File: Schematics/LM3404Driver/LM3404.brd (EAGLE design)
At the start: 103.8 x 106.7 mm, 62 parts, among them IC1 LM3404, IC2 LM3404, IC3 LM3404, IC4 LM3404, IC5 LM3404, IC6 LM3404

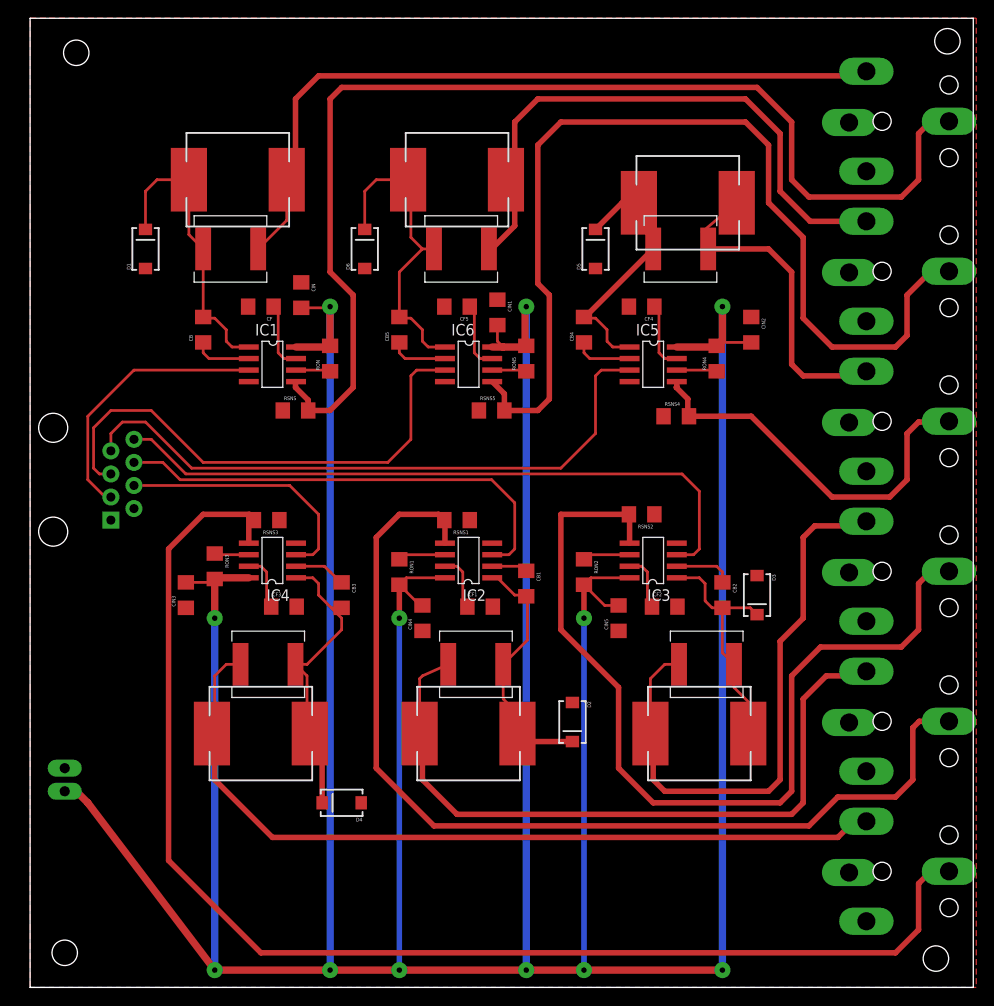
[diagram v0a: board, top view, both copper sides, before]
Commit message: Update power driver board to smt RJ45 and correct ground pins
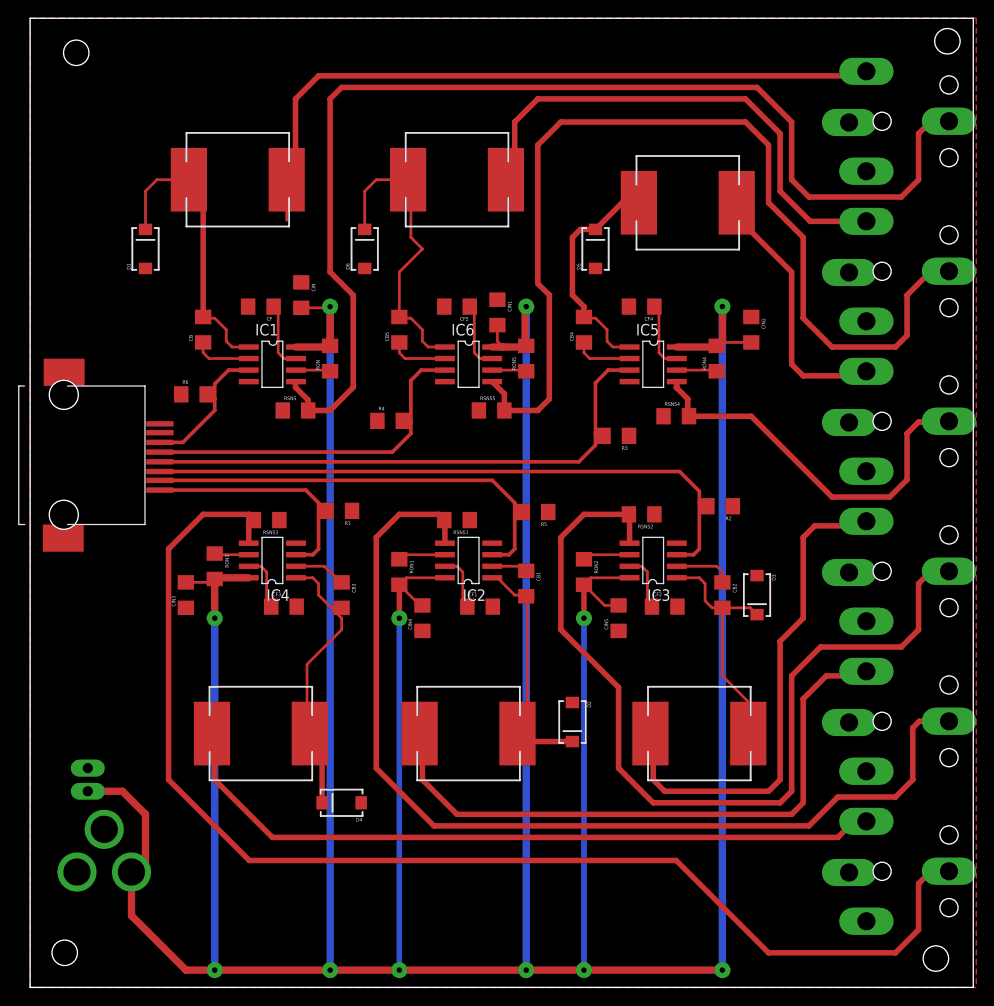
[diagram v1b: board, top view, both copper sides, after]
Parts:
- removed L1, L11, L3, L5, L7, L9: 47uH, SparkFun-Passives:CR75
- added J1: POWER_JACKPTH, SparkFun-Connectors:POWER_JACK_PTH
- added R1, R2, R3, R4, R5, R6: 4.7K, SparkFun-Resistors:1206
- U$1: value RJ45-8PTH -> MOLEX-RJ45-SMT; device SparkFun-Connectors:RJ45-8 -> SMD-RJ45:MOLEX-RJ45-SMT
- moved U$1 2.84 mm to (3.81, 58.4), flipped to the top, turned to 0 degrees
- moved POWER 2.54 mm to (6.35, 24.1)
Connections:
- net GND: now also J1.GND, J1.GNDBREAK, R1.1, R2.1, R3.1, R4.1, R5.1, R6.1
- net N$11: no longer L3.P$1
- net N$14: no longer L3.P$2
- net N$15: now also R2.2, U$1.6; no longer U$1.8
- net N$18: no longer L5.P$1
- net N$21: no longer L5.P$2
- net N$22: now also R1.2, U$1.8; no longer U$1.4
- net N$25: no longer L7.P$1
- net N$28: no longer L7.P$2
- net N$29: now also R3.2, U$1.5; no longer U$1.7
- net N$3: now also R5.2, U$1.7; no longer U$1.6
- net N$32: no longer L9.P$1
- net N$35: no longer L9.P$2
- net N$36: now also R4.2, U$1.4; no longer U$1.5
- net N$39: no longer L11.P$1
- net N$4: no longer L1.P$1
- net N$42: no longer L11.P$2
- net N$8: now also R6.2
- net N$9: no longer L1.P$2
- net VIN: now also J1.PWR
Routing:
- net N$36: track 56.7 -> 39.5 mm
- net N$8: track 30.1 -> 15.9 mm
- net N$21: track 67.5 -> 57.7 mm
- net N$14: track 78.5 -> 68.9 mm
- net N$29: track 69.8 -> 60.9 mm
- net N$28: track 90.2 -> 82.1 mm
- net N$42: track 65.5 -> 57.5 mm
- net N$35: track 39.3 -> 32.2 mm
- net VIN: track 491.0 -> 496.5 mm
- net N$27: track 147.5 -> 142.3 mm
- net N$9: track 82.3 -> 77.9 mm
- net N$15: track 73.7 -> 70.6 mm
- net N$3: track 51.6 -> 48.9 mm
- net N$25: track 33.0 -> 31.2 mm
- net N$20: track 100.2 -> 98.7 mm
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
